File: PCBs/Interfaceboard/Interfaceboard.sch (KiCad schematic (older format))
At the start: 0 parts

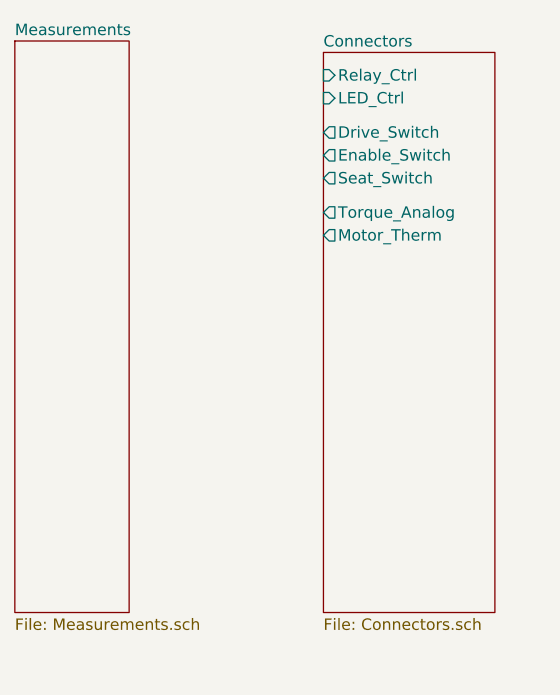
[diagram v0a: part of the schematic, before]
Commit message: Added multiple connectors, still lacking a few. Started work on measurement circuits for interface board.
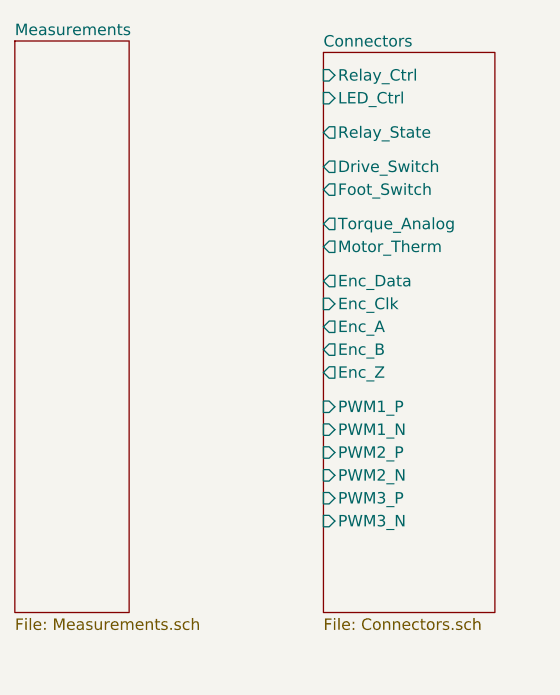
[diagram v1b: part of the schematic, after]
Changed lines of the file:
@@
 $Descr A4 11693 8268
 encoding utf-8
-Sheet 1 7
+Sheet 1 8
 Title "Interface Board for Control of PMAC Motor in Electric Go-Kart"
 Date "2021-02-19"
@@
 Comment4 ""
 $EndDescr
-$Sheet
-S 7250 1550 750  2450
-U 602F953D
-F0 "Connectors" 50
-F1 "Connectors.sch" 50
-F2 "Relay_Ctrl" I L 7250 1650 50
-F3 "LED_Ctrl" I L 7250 1750 50
-F4 "Drive_Switch" O L 7250 1900 50
-F5 "Enable_Switch" O L 7250 2000 50
-F6 "Torque_Analog" O L 7250 2250 50
-F7 "Seat_Switch" O L 7250 2100 50
-F8 "Motor_Therm" O L 7250 2350 50
-$EndSheet
 $Sheet
 S 5900 1500 500  2500
@@
 F1 "PWM.sch" 50
 $EndSheet
+$Sheet
+S 7250 1550 750  2450
+U 602F953D
+F0 "Connectors" 50
+F1 "Connectors.sch" 50
+F2 "Relay_Ctrl" I L 7250 1650 50
+F3 "LED_Ctrl" I L 7250 1750 50
+F4 "Drive_Switch" O L 7250 2050 50
+F5 "Foot_Switch" O L 7250 2150 50
+F6 "Torque_Analog" O L 7250 2300 50
+F7 "Motor_Therm" O L 7250 2400 50
+F8 "Relay_State" O L 7250 1900 50
+F9 "Enc_Data" O L 7250 2550 50
+F10 "Enc_Clk" I L 7250 2650 50
+F11 "Enc_A" O L 7250 2750 50
+F12 "Enc_B" O L 7250 2850 50
+F13 "Enc_Z" O L 7250 2950 50
+F14 "PWM1_P" I L 7250 3100 50
+F15 "PWM1_N" I L 7250 3200 50
+F16 "PWM2_P" I L 7250 3300 50
+F17 "PWM2_N" I L 7250 3400 50
+F18 "PWM3_P" I L 7250 3500 50
+F19 "PWM3_N" I L 7250 3600 50
+$EndSheet
 $EndSCHEMATC

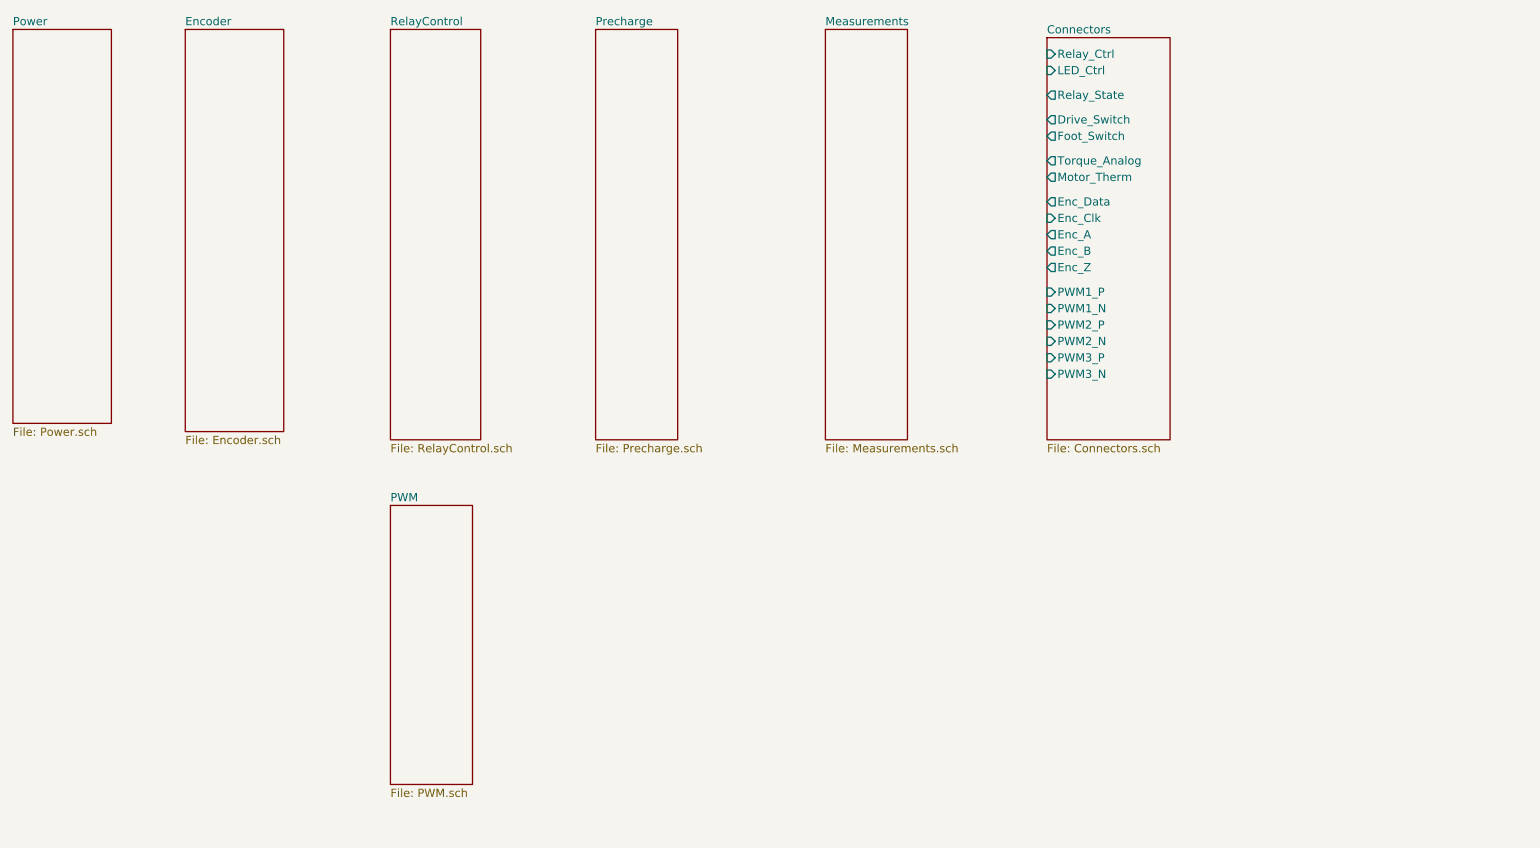
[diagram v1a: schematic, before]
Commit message: Added most circuits from Interface schematic provided by Rakesh. Lacks a few connectors, transistors, and optocouplers. Needs connections for Zybo. Awaiting feedback from meeting with Rakesh.
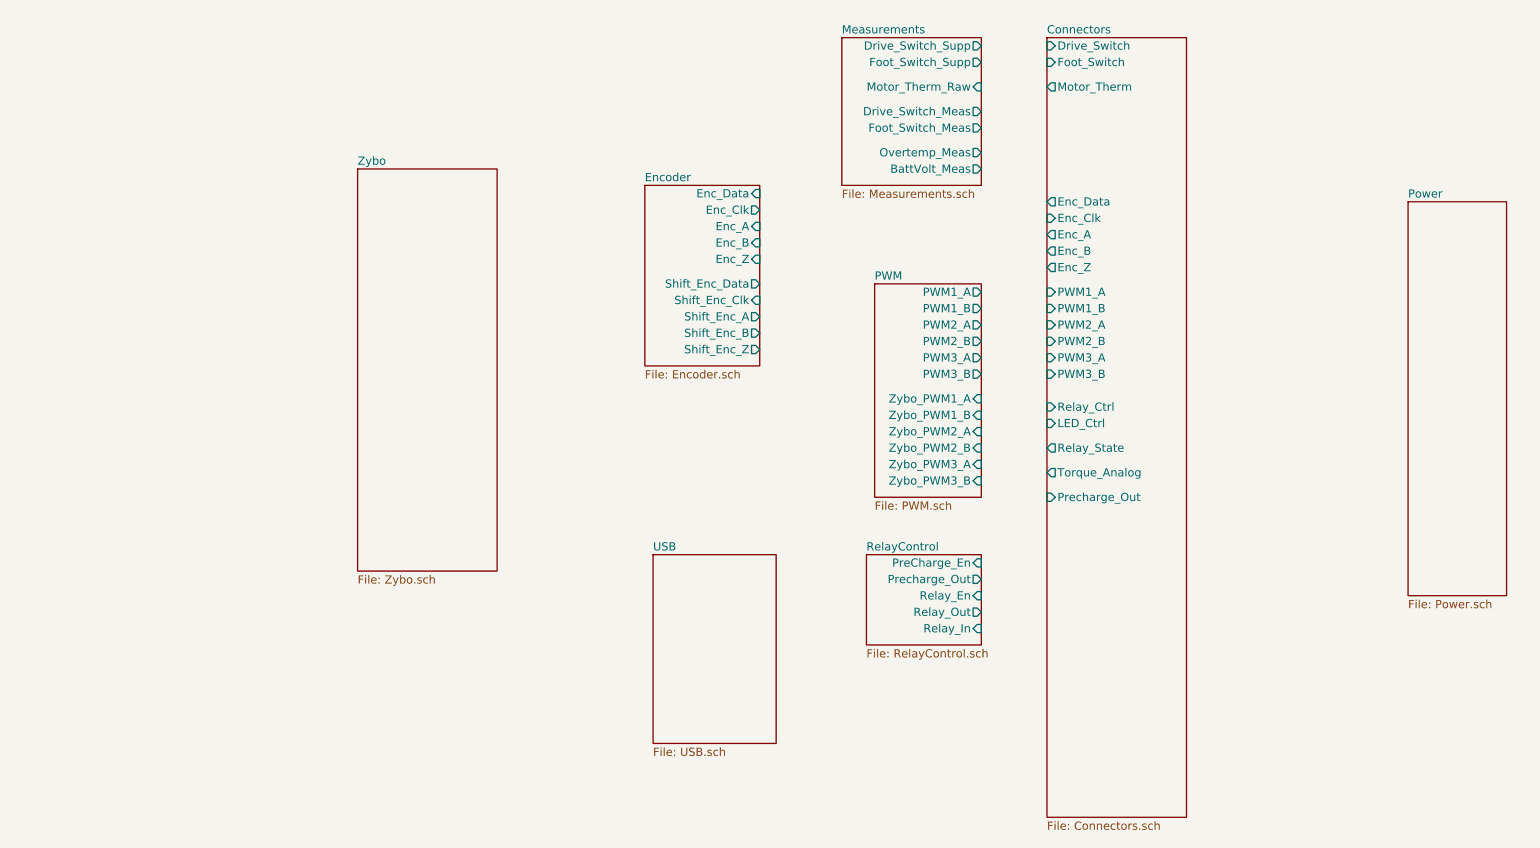
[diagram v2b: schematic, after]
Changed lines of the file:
@@
 $Descr A4 11693 8268
 encoding utf-8
-Sheet 1 8
+Sheet 1 9
 Title "Interface Board for Control of PMAC Motor in Electric Go-Kart"
-Date "2021-02-19"
+Date "2021-02-23"
 Rev "Version 1"
 Comp "University of Southern Denmark"
@@
 $EndDescr
 $Sheet
-S 5900 1500 500  2500
+S 6000 1550 850  900
 U 603038A4
 F0 "Measurements" 50
 F1 "Measurements.sch" 50
+F2 "Drive_Switch_Meas" O R 6850 2000 50
+F3 "Foot_Switch_Meas" O R 6850 2100 50
+F4 "Motor_Therm_Raw" I R 6850 1850 50
+F5 "Overtemp_Meas" O R 6850 2250 50
+F6 "BattVolt_Meas" O R 6850 2350 50
+F7 "Drive_Switch_Supp" O R 6850 1600 50
+F8 "Foot_Switch_Supp" O R 6850 1700 50
 $EndSheet
 $Sheet
-S 4500 1500 500  2500
-U 60303A2D
-F0 "Precharge" 50
-F1 "Precharge.sch" 50
-$EndSheet
-$Sheet
-S 3250 1500 550  2500
+S 6150 4700 700  550
 U 60303AF1
 F0 "RelayControl" 50
 F1 "RelayControl.sch" 50
+F2 "PreCharge_En" I R 6850 4750 50
+F3 "Precharge_Out" O R 6850 4850 50
+F4 "Relay_En" I R 6850 4950 50
+F5 "Relay_Out" O R 6850 5050 50
+F6 "Relay_In" I R 6850 5150 50
 $EndSheet
 $Sheet
-S 2000 1500 600  2450
+S 4800 2450 700  1100
 U 60303BF1
 F0 "Encoder" 50
 F1 "Encoder.sch" 50
+F2 "Enc_Data" I R 5500 2500 50
+F3 "Enc_Clk" O R 5500 2600 50
+F4 "Enc_A" I R 5500 2700 50
+F5 "Enc_B" I R 5500 2800 50
+F6 "Enc_Z" I R 5500 2900 50
+F7 "Shift_Enc_Data" O R 5500 3050 50
+F8 "Shift_Enc_Clk" I R 5500 3150 50
+F9 "Shift_Enc_A" O R 5500 3250 50
+F10 "Shift_Enc_B" O R 5500 3350 50
+F11 "Shift_Enc_Z" O R 5500 3450 50
 $EndSheet
 $Sheet
-S 950  1500 600  2400
+S 9450 2550 600  2400
 U 60303C76
 F0 "Power" 50
@@
 $EndSheet
 $Sheet
-S 3250 4400 500  1700
+S 6200 3050 650  1300
 U 60303CF2
 F0 "PWM" 50
 F1 "PWM.sch" 50
+F2 "PWM1_A" O R 6850 3100 50
+F3 "PWM1_B" O R 6850 3200 50
+F4 "PWM2_A" O R 6850 3300 50
+F5 "PWM2_B" O R 6850 3400 50
+F6 "PWM3_A" O R 6850 3500 50
+F7 "PWM3_B" O R 6850 3600 50
+F8 "Zybo_PWM1_A" I R 6850 3750 50
+F9 "Zybo_PWM1_B" I R 6850 3850 50
+F10 "Zybo_PWM2_A" I R 6850 3950 50
+F11 "Zybo_PWM2_B" I R 6850 4050 50
+F12 "Zybo_PWM3_A" I R 6850 4150 50
+F13 "Zybo_PWM3_B" I R 6850 4250 50
 $EndSheet
 $Sheet
-S 7250 1550 750  2450
+S 7250 1550 850  4750
 U 602F953D
 F0 "Connectors" 50
 F1 "Connectors.sch" 50
-F2 "Relay_Ctrl" I L 7250 1650 50
-F3 "LED_Ctrl" I L 7250 1750 50
-F4 "Drive_Switch" O L 7250 2050 50
-F5 "Foot_Switch" O L 7250 2150 50
-F6 "Torque_Analog" O L 7250 2300 50
-F7 "Motor_Therm" O L 7250 2400 50
-F8 "Relay_State" O L 7250 1900 50
-F9 "Enc_Data" O L 7250 2550 50
-F10 "Enc_Clk" I L 7250 2650 50
-F11 "Enc_A" O L 7250 2750 50
-F12 "Enc_B" O L 7250 2850 50
-F13 "Enc_Z" O L 7250 2950 50
-F14 "PWM1_P" I L 7250 3100 50
-F15 "PWM1_N" I L 7250 3200 50
-F16 "PWM2_P" I L 7250 3300 50
-F17 "PWM2_N" I L 7250 3400 50
-F18 "PWM3_P" I L 7250 3500 50
-F19 "PWM3_N" I L 7250 3600 50
+F2 "Relay_Ctrl" I L 7250 3800 50
+F3 "LED_Ctrl" I L 7250 3900 50
+F4 "Torque_Analog" O L 7250 4200 50
+F5 "Motor_Therm" O L 7250 1850 50
+F6 "Relay_State" O L 7250 4050 50
+F7 "Enc_Data" O L 7250 2550 50
+F8 "Enc_Clk" I L 7250 2650 50
+F9 "Enc_A" O L 7250 2750 50
+F10 "Enc_B" O L 7250 2850 50
+F11 "Enc_Z" O L 7250 2950 50
+F12 "PWM1_A" I L 7250 3100 50
+F13 "PWM1_B" I L 7250 3200 50
+F14 "PWM2_A" I L 7250 3300 50
+F15 "PWM2_B" I L 7250 3400 50
+F16 "PWM3_A" I L 7250 3500 50
+F17 "PWM3_B" I L 7250 3600 50
+F18 "Foot_Switch" I L 7250 1700 50
+F19 "Drive_Switch" I L 7250 1600 50
+F20 "Precharge_Out" I L 7250 4350 50
+$EndSheet
+$Sheet
+S 4850 4700 750  1150
+U 605FDA0C
+F0 "USB" 50
+F1 "USB.sch" 50
+$EndSheet
+$Sheet
+S 3050 2350 850  2450
+U 6034EC45
+F0 "Zybo" 50
+F1 "Zybo.sch" 50
 $EndSheet
 $EndSCHEMATC

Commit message: Removed interface board, added analog interface board.
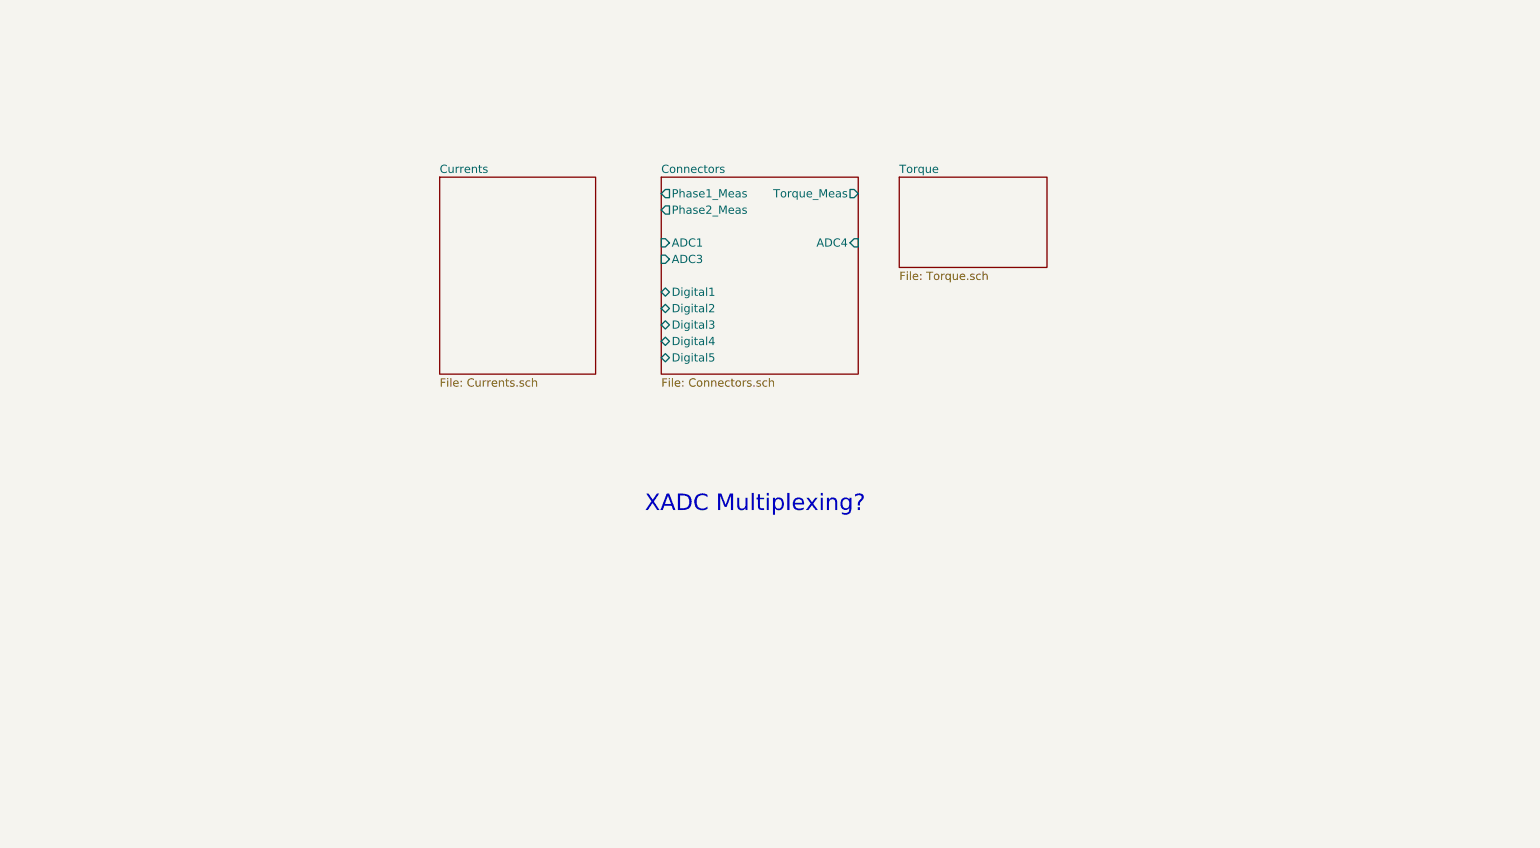
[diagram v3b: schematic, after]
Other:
- note added: "XADC Multiplexing?"
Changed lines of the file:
@@
 $Descr A4 11693 8268
 encoding utf-8
-Sheet 1 9
+Sheet 1 4
 Title "Interface Board for Control of PMAC Motor in Electric Go-Kart"
-Date "2021-02-23"
+Date "2021-03-04"
 Rev "Version 1"
 Comp "University of Southern Denmark"
@@
 $EndDescr
 $Sheet
-S 6000 1550 850  900
-U 603038A4
-F0 "Measurements" 50
-F1 "Measurements.sch" 50
-F2 "Drive_Switch_Meas" O R 6850 2000 50
-F3 "Foot_Switch_Meas" O R 6850 2100 50
-F4 "Motor_Therm_Raw" I R 6850 1850 50
-F5 "Overtemp_Meas" O R 6850 2250 50
-F6 "BattVolt_Meas" O R 6850 2350 50
-F7 "Drive_Switch_Supp" O R 6850 1600 50
-F8 "Foot_Switch_Supp" O R 6850 1700 50
+S 4900 2400 1200 1200
+U 6040B42D
+F0 "Connectors" 50
+F1 "Connectors.sch" 50
+F2 "Phase1_Meas" O L 4900 2500 50
+F3 "Phase2_Meas" O L 4900 2600 50
+F4 "Torque_Meas" O R 6100 2500 50
+F5 "ADC1" I L 4900 2800 50
+F6 "ADC3" I L 4900 2900 50
+F7 "ADC4" I R 6100 2800 50
+F8 "Digital1" B L 4900 3100 50
+F9 "Digital2" B L 4900 3200 50
+F10 "Digital3" B L 4900 3300 50
+F11 "Digital4" B L 4900 3400 50
+F12 "Digital5" B L 4900 3500 50
 $EndSheet
 $Sheet
-S 6150 4700 700  550
-U 60303AF1
-F0 "RelayControl" 50
-F1 "RelayControl.sch" 50
-F2 "PreCharge_En" I R 6850 4750 50
-F3 "Precharge_Out" O R 6850 4850 50
-F4 "Relay_En" I R 6850 4950 50
-F5 "Relay_Out" O R 6850 5050 50
-F6 "Relay_In" I R 6850 5150 50
+S 3550 2400 950  1200
+U 6040B450
+F0 "Currents" 50
+F1 "Currents.sch" 50
 $EndSheet
 $Sheet
-S 4800 2450 700  1100
-U 60303BF1
-F0 "Encoder" 50
-F1 "Encoder.sch" 50
-F2 "Enc_Data" I R 5500 2500 50
-F3 "Enc_Clk" O R 5500 2600 50
-F4 "Enc_A" I R 5500 2700 50
-F5 "Enc_B" I R 5500 2800 50
-F6 "Enc_Z" I R 5500 2900 50
-F7 "Shift_Enc_Data" O R 5500 3050 50
-F8 "Shift_Enc_Clk" I R 5500 3150 50
-F9 "Shift_Enc_A" O R 5500 3250 50
-F10 "Shift_Enc_B" O R 5500 3350 50
-F11 "Shift_Enc_Z" O R 5500 3450 50
+S 6350 2400 900  550
+U 6040B46E
+F0 "Torque" 50
+F1 "Torque.sch" 50
 $EndSheet
-$Sheet
-S 9450 2550 600  2400
-U 60303C76
-F0 "Power" 50
-F1 "Power.sch" 50
-$EndSheet
-$Sheet
-S 6200 3050 650  1300
-U 60303CF2
-F0 "PWM" 50
-F1 "PWM.sch" 50
-F2 "PWM1_A" O R 6850 3100 50
-F3 "PWM1_B" O R 6850 3200 50
-F4 "PWM2_A" O R 6850 3300 50
-F5 "PWM2_B" O R 6850 3400 50
-F6 "PWM3_A" O R 6850 3500 50
-F7 "PWM3_B" O R 6850 3600 50
-F8 "Zybo_PWM1_A" I R 6850 3750 50
-F9 "Zybo_PWM1_B" I R 6850 3850 50
-F10 "Zybo_PWM2_A" I R 6850 3950 50
-F11 "Zybo_PWM2_B" I R 6850 4050 50
-F12 "Zybo_PWM3_A" I R 6850 4150 50
-F13 "Zybo_PWM3_B" I R 6850 4250 50
-$EndSheet
-$Sheet
-S 7250 1550 850  4750
-U 602F953D
-F0 "Connectors" 50
-F1 "Connectors.sch" 50
-F2 "Relay_Ctrl" I L 7250 3800 50
-F3 "LED_Ctrl" I L 7250 3900 50
-F4 "Torque_Analog" O L 7250 4200 50
-F5 "Motor_Therm" O L 7250 1850 50
-F6 "Relay_State" O L 7250 4050 50
-F7 "Enc_Data" O L 7250 2550 50
-F8 "Enc_Clk" I L 7250 2650 50
-F9 "Enc_A" O L 7250 2750 50
-F10 "Enc_B" O L 7250 2850 50
-F11 "Enc_Z" O L 7250 2950 50
-F12 "PWM1_A" I L 7250 3100 50
-F13 "PWM1_B" I L 7250 3200 50
-F14 "PWM2_A" I L 7250 3300 50
-F15 "PWM2_B" I L 7250 3400 50
-F16 "PWM3_A" I L 7250 3500 50
-F17 "PWM3_B" I L 7250 3600 50
-F18 "Foot_Switch" I L 7250 1700 50
-F19 "Drive_Switch" I L 7250 1600 50
-F20 "Precharge_Out" I L 7250 4350 50
-$EndSheet
-$Sheet
-S 4850 4700 750  1150
-U 605FDA0C
-F0 "USB" 50
-F1 "USB.sch" 50
-$EndSheet
-$Sheet
-S 3050 2350 850  2450
-U 6034EC45
-F0 "Zybo" 50
-F1 "Zybo.sch" 50
-$EndSheet
+Text Notes 4800 4450 0    100  ~ 0
+XADC Multiplexing?
 $EndSCHEMATC

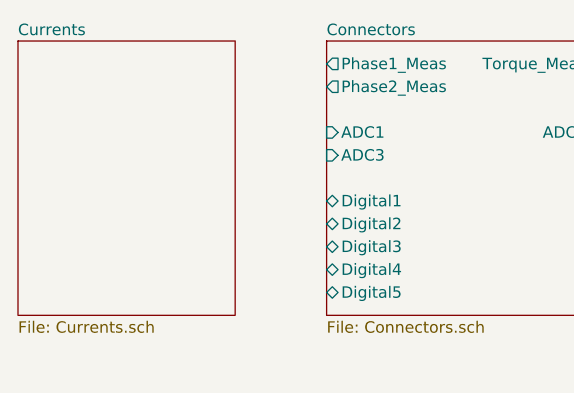
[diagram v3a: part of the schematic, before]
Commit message: Added analog board hierarchial sheets. Started work on connectors, supply, and in amp for phase current measurements.
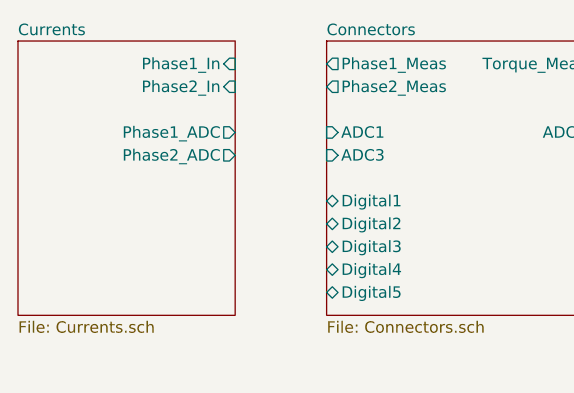
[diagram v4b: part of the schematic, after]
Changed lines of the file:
@@
 F0 "Currents" 50
 F1 "Currents.sch" 50
+F2 "Phase1_In" I R 4500 2500 50
+F3 "Phase2_In" I R 4500 2600 50
+F4 "Phase1_ADC" O R 4500 2800 50
+F5 "Phase2_ADC" O R 4500 2900 50
 $EndSheet
 $Sheet
